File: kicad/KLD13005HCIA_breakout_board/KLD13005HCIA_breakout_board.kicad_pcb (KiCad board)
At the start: 2 copper layers, 34 x 38 mm, 7 parts, among them J1 Pin Headers, J2 Conn_01x24_Male, J3 Capacitive Touch Sensor, Q1 Q_NMOS_GSD

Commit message: Finish initial PCB design
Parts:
- moved J3 11.2 mm to (105.7, 68.6), turned to 0 degrees
- moved R2 11.0 mm to (91.0, 65.7), turned to 270 degrees
- moved Q1 10.4 mm to (85.3, 64.9)
- moved R1 10.4 mm to (88.6, 66.4)
- moved J2 10.4 mm to (93.8, 70.9)
- moved R3 10.4 mm to (87.9, 63.0)
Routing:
- net /I2C_SDA: track 47.4 -> 29.5 mm, vias 0 -> 1
- net /CAPSENS_INT: track 47.7 -> 30.6 mm, vias 0 -> 1
- net /I2C_SCL: track 47.2 -> 30.3 mm, vias 0 -> 1
- net /LCD_BLITE: track 22.4 -> 36.3 mm
- net /LCD_DC: track 26.4 -> 36.4 mm, vias 2 -> 0
- net /SDI: track 32.6 -> 26.6 mm, vias 2 -> 0
- net /D_C: track 28.3 -> 26.4 mm, vias 2 -> 0
- net /CS: track 27.2 -> 28.9 mm, vias 2 -> 1
- net +3V3: track 5.02 -> 5.72 mm
- added copper zone on In1.Cu, net +3V3
- added copper zone on In2.Cu, net GND
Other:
- copper layers 2 -> 4

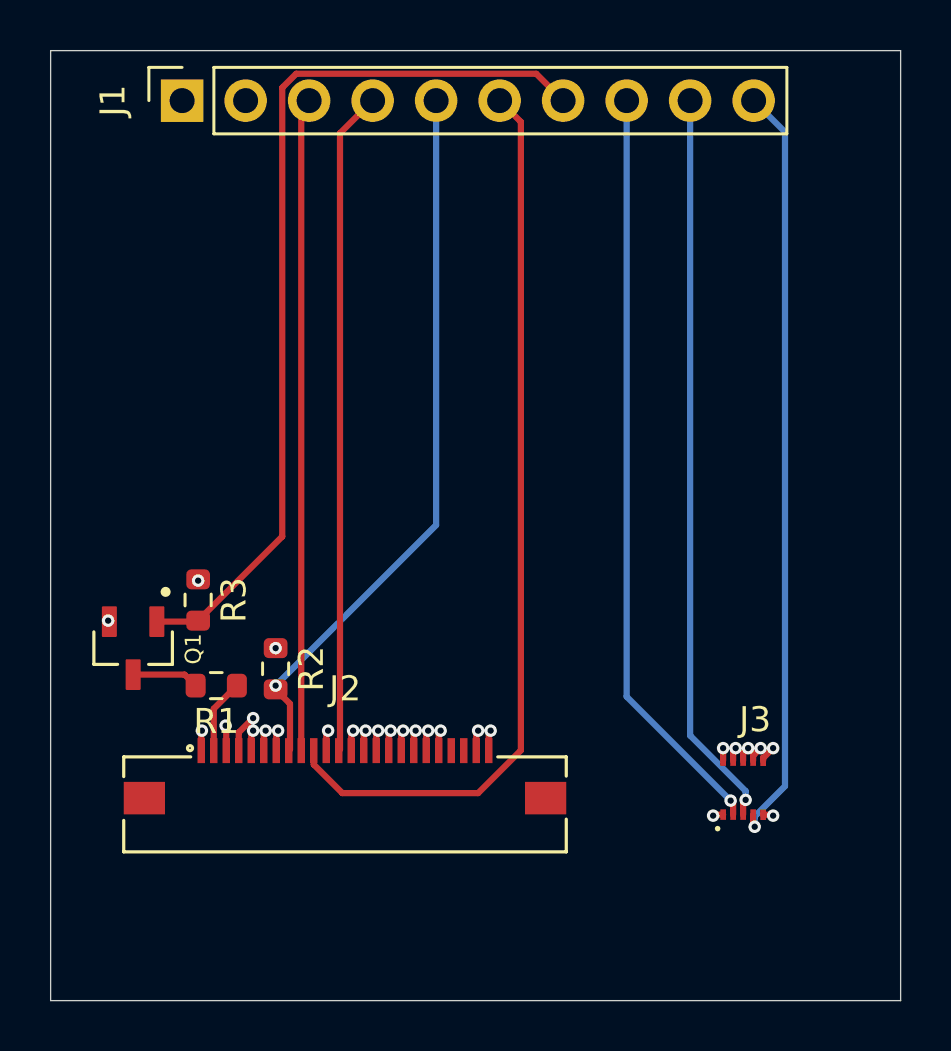
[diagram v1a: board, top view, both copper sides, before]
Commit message: Update schematic. Move connector position
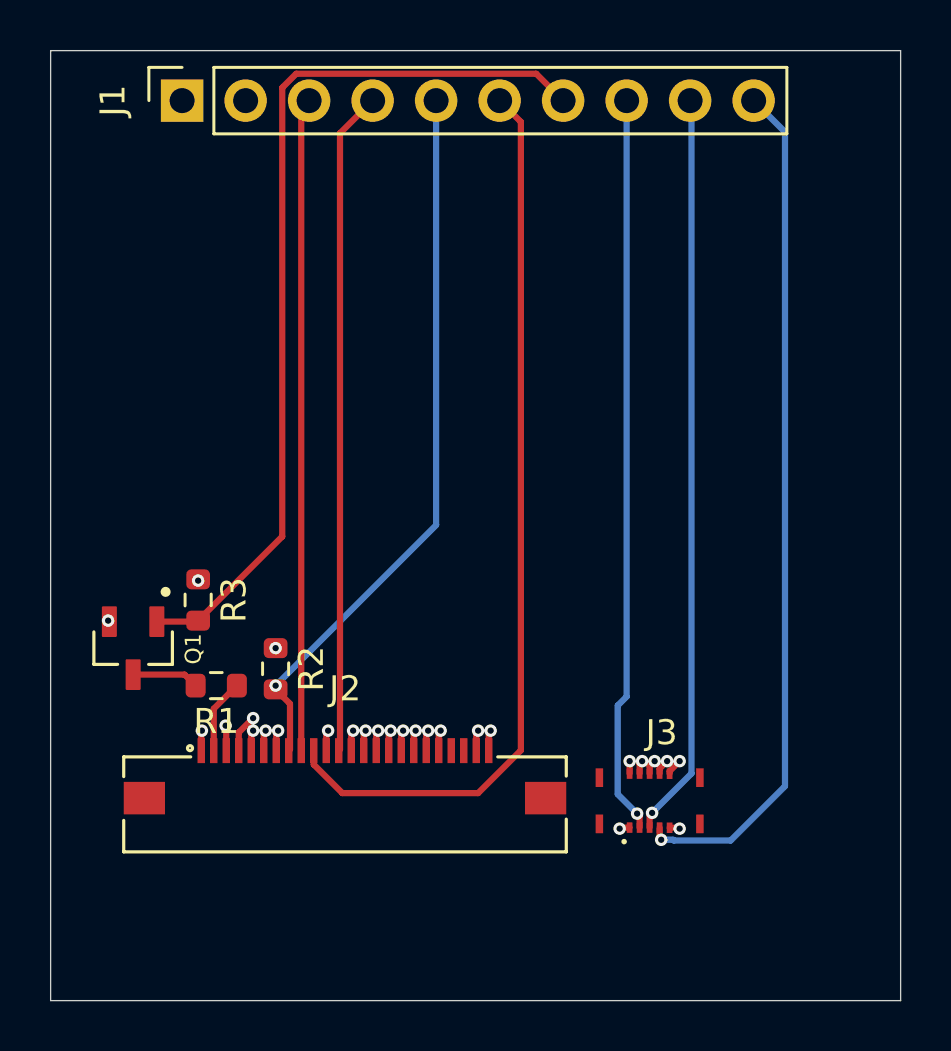
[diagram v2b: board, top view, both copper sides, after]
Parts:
- moved J3 3.78 mm to (102.0, 69.1)
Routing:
- net /CAPSENS_INT: track 30.6 -> 34.3 mm
- net /I2C_SCL: track 30.3 -> 29.6 mm

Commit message: Fix pin arrangement for capacitive touch sensor. Rename D/C pin to SCK
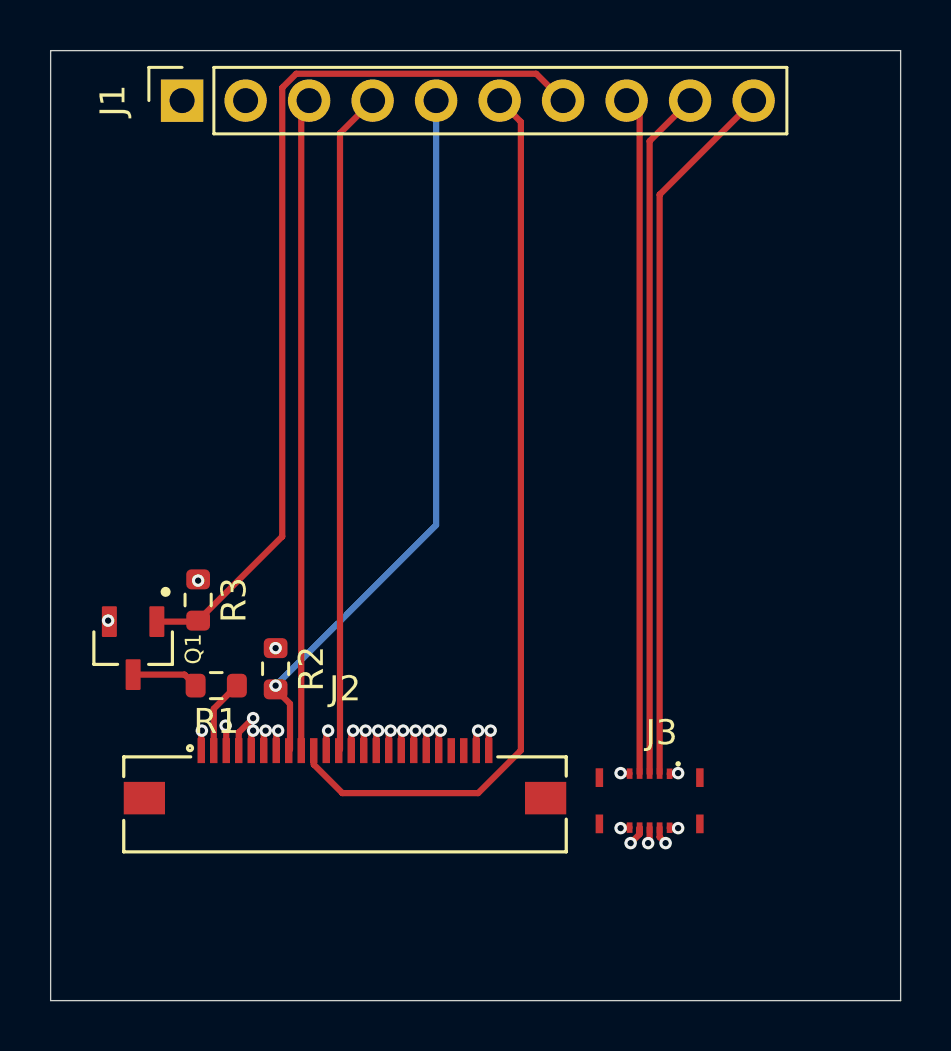
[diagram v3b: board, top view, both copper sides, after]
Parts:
- R1: value 10K -> 10
- R3: value 2.5K -> 2.2K
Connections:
- J1 pad 10: /CAPSENS_INT -> /I2C_SCL
- J1 pad 8: /I2C_SCL -> /CAPSENS_INT
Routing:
- net /CAPSENS_INT: track 34.3 -> 27.1 mm, vias 1 -> 0
- net /I2C_SDA: track 29.8 -> 27.7 mm, vias 1 -> 0
- net /I2C_SCL: track 29.6 -> 28.5 mm, vias 1 -> 0
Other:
- board text added: "3.3V"
- board text added: "BLITE"
- board text added: "CS"
- board text added: "DC"
- board text added: "GND"
- board text added: "INT"
- board text added: "SCK"
- board text added: "SCL"
- board text added: "SDA"
- board text added: "SDI"

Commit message: Swap INT and SDC pin labels. Add two 10K pull-up resistors for I2C communication
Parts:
- added R4: 10K, Resistor_SMD:R_0603_1608Metric, F.Cu at (108.2, 47.7)
- added R5: 10K, Resistor_SMD:R_0603_1608Metric, F.Cu at (103.7, 47.7)
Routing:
- net /I2C_SDA: track 27.7 -> 33.6 mm, vias 0 -> 1
- net /I2C_SCL: track 28.5 -> 29.5 mm
- net +3V3: track 5.61 -> 5.71 mm, vias 9 -> 11
